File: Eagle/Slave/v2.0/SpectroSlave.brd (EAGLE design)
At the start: 21.6 x 21.8 mm, 15 parts, among them X1 FH12-08S-1SH

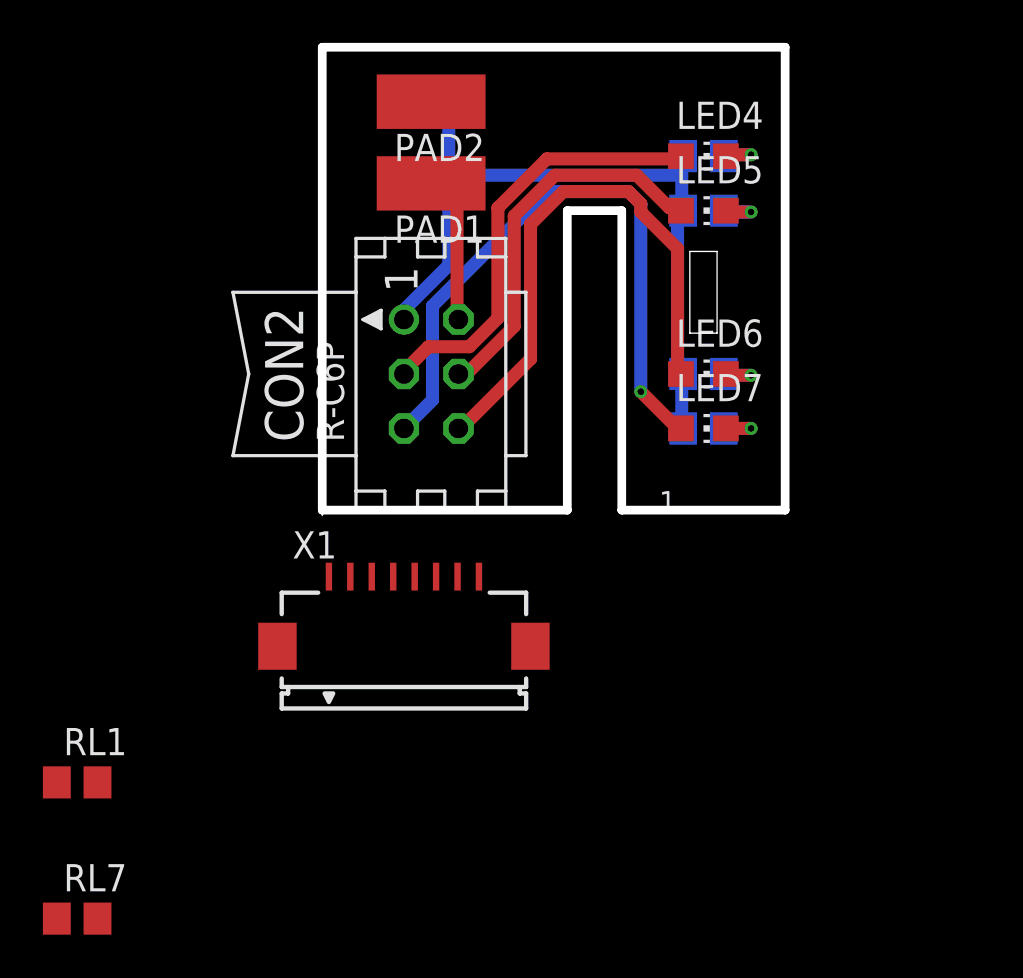
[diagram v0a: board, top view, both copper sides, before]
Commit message: New spectrophotometer board
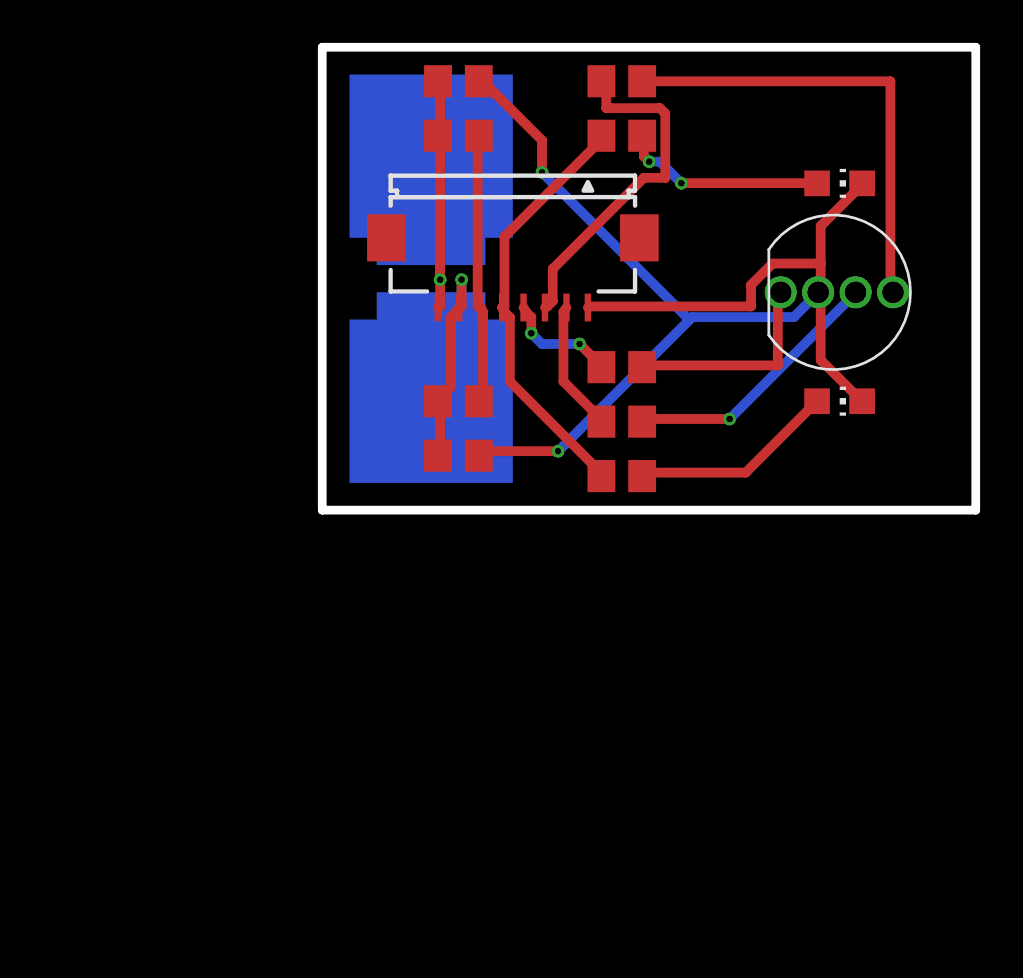
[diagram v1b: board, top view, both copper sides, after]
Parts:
- removed CON2: (no value), con-harting:CON06L
- removed LED4: BLUE, led:CHIP-LED0805
- removed LED6: GREEN, led:CHIP-LED0805
- removed LED7: RED, led:CHIP-LED0805
- added C1, C2: 100pF, rcl:C0805
- added LED1: WHITE, led:CHIP-LED0805
- added U$1: RGB-COMMON-CATHODE, lpatiny:LED-TRICOLOR-THROUGHHOLE
- RL1, RL7: value 1K -> 1M
- RL2, RL4: value 1K -> 150
- RL3, RL5, RL6: value 1K -> 100
- moved RL1 35.0 mm to (6.35, 17.5), turned to 180 degrees
- moved RL7 30.0 mm to (6.35, 5.08), turned to 180 degrees
- moved X1 19.7 mm to (8.89, 12.7), turned to 180 degrees
- moved RL6 19.6 mm to (14.0, 1.59), flipped to the top, turned to 180 degrees
- moved RL3 16.6 mm to (14.0, 20.0), flipped to the top, turned to 180 degrees
- moved RL2 10.6 mm to (14.0, 6.67), flipped to the top, turned to 180 degrees
- moved LED5 6.48 mm to (24.1, 15.2)
- moved PAD2 6.35 mm to (5.08, 12.7), flipped to the bottom
- moved PAD1 6.35 mm to (5.08, 8.89), flipped to the bottom
- moved RL5 5.17 mm to (14.0, 17.5), flipped to the top
- moved RL4 4.41 mm to (14.0, 4.13), flipped to the top, turned to 0 degrees
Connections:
- removed net N$10: LED5.C, RL5.2
- removed net N$6: LED4.C, RL2.1
- removed net N$7: CON2.3, LED4.A
- removed net N$9: CON2.5, LED7.A
- new net BLUE: RL2.2, X1.4
- new net GREEN: RL3.2, X1.3
- new net PULSE: RL1.1, RL7.1, X1.6
- new net RED: RL4.1, X1.2
- new net SENS1: C2.1, PAD1.1, RL7.2, X1.7
- new net SENS2: C1.1, PAD2.1, RL1.2, X1.8
- new net WHITE: RL5.2, RL6.2, X1.5
- net GND: now also C1.2, C2.2, LED1.C, LED5.C, U$1.GND, X1.1; no longer CON2.1, RL2.2, RL3.2, RL4.1, RL5.1, RL6.1, X1.5
- net N$1: now also RL4.2, U$1.GRN; no longer CON2.4, LED5.A
- net N$2: now also RL3.1, U$1.BLU; no longer CON2.6, LED6.A
- net N$3: now also RL2.1, U$1.RED; no longer LED6.C, RL4.2
- net N$4: now also LED5.A, RL5.1; no longer CON2.2
- net N$5: now also LED1.A, RL6.1; no longer LED7.C, RL3.1
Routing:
- net N$9: track 29.8 -> 0.00 mm, vias 1 -> 0
- net GND: track 35.2 -> 58.4 mm, vias 0 -> 2
- net N$7: track 20.2 -> 0.00 mm
- net WHITE: track 0.00 -> 19.7 mm
- net GREEN: track 0.00 -> 16.3 mm
- net SENS2: track 0.00 -> 13.1 mm, vias 0 -> 1
- net PULSE: track 0.00 -> 12.6 mm
- net SENS1: track 0.00 -> 11.9 mm, vias 0 -> 1
- net N$3: track 2.50 -> 9.82 mm, vias 1 -> 0
- net N$5: track 2.45 -> 9.64 mm, vias 1 -> 0
- net RED: track 0.00 -> 6.09 mm
- net N$1: track 17.9 -> 12.5 mm, vias 0 -> 1
- net BLUE: track 0.00 -> 5.29 mm, vias 0 -> 2
- net N$2: track 25.7 -> 21.5 mm
- net N$4: track 6.85 -> 9.58 mm, vias 0 -> 2
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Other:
- board size 21.6 x 21.8 mm -> 30.5 x 21.6 mm
- board text removed: "1"
